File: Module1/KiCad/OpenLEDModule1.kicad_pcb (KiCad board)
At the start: 2 copper layers, 29.2 x 29.2 mm, 8 parts, among them P1 CONN_01X02, P2 CONN_01X02

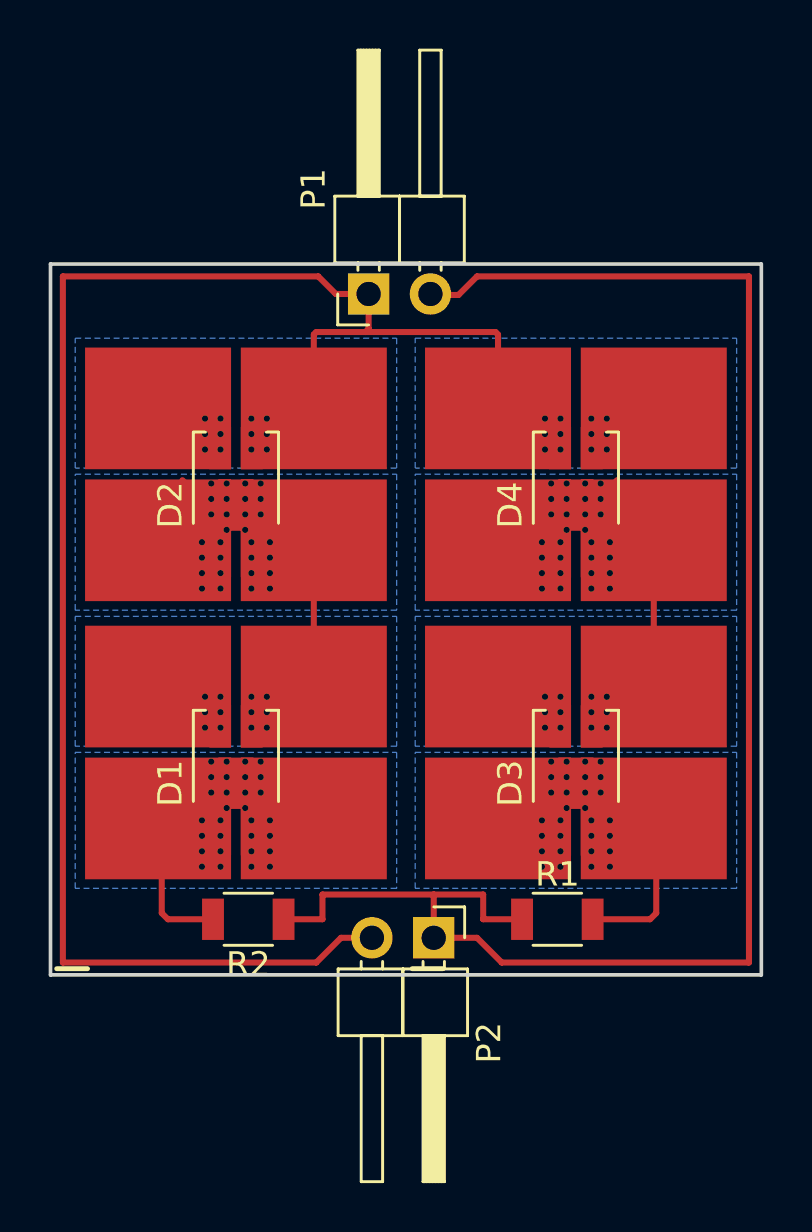
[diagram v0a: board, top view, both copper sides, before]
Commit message: Added GND filling on Module 1/2. Added Gerbers.
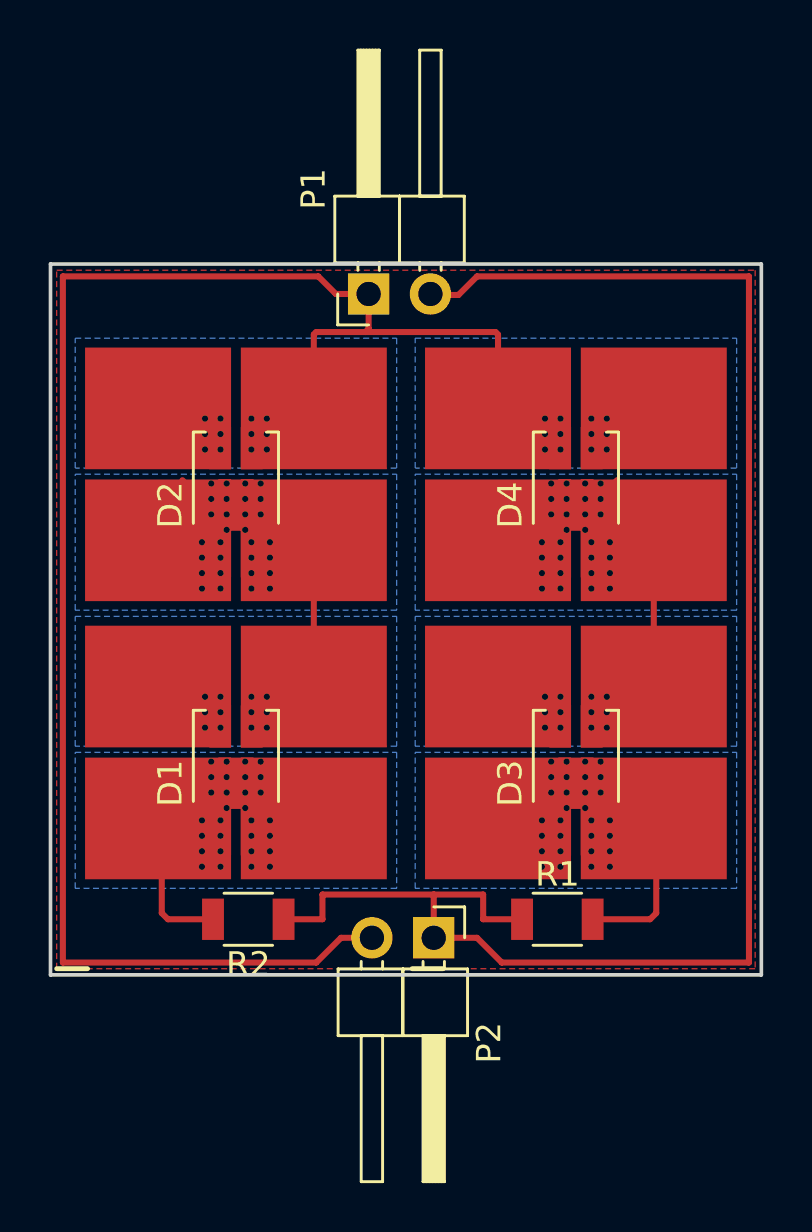
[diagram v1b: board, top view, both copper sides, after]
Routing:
- added copper zone on F.Cu, net GND
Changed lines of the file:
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@@
   (general
     (links 38)
-    (no_connects 10)
+    (no_connects 8)
     (area 137.084999 60.604359 166.445001 108.011001)
     (thickness 1.6)
@@
       (linewidth 0.100000)
       (plotframeref false)
-      (viasonmask false)
+      (viasonmask true)
       (mode 1)
       (useauxorigin false)
@@
       (outputformat 1)
       (mirror false)
-      (drillshape 1)
+      (drillshape 0)
       (scaleselection 1)
       (outputdirectory ""))
@@
       )
     )
+  )
+  (zone (net 1) (net_name GND) (layer F.Cu) (hatch edge 0.508)
+    (connect_pads (clearance 0.508))
+    (min_thickness 0.254)
+    (fill yes (arc_segments 16) (thermal_gap 0.508) (thermal_bridge_width 0.508))
+    (polygon
+      (pts
+        (xy 166.116 98.806) (xy 137.414 98.806) (xy 137.414 70.104) (xy 166.116 70.104)
+      )
+    )
